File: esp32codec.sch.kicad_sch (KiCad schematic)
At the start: 8 parts, among them U13 TL072, U4 NAU88C22YG

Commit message: latest version
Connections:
- net Left IN: now reaches U4.3 (LLIN/GPIO2)
- net RIN: now reaches U4.6 (RLIN/GPIO3)
- net BCLK renamed i2sbclk
- net MLCK renamed i2s_lrck
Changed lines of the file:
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@@
+	(wire
+		(pts
+			(xy 85.09 95.25) (xy 93.98 95.25)
+		)
+		(stroke
+			(width 0)
+			(type default)
+		)
+	)
 	(wire
 		(pts
@@
 	(wire
 		(pts
+			(xy 80.01 97.79) (xy 93.98 97.79)
+		)
+		(stroke
+			(width 0)
+			(type default)
+		)
+	)
+	(wire
+		(pts
 			(xy 168.91 88.9) (xy 168.91 77.47)
 		)
@@
 		)
 	)
+	(hierarchical_label "RIN"
+		(shape input)
+		(at 80.01 97.79 180)
+		(effects
+			(font
+				(size 1.27 1.27)
+			)
+			(justify right)
+		)
+	)
 	(hierarchical_label "LRCK"
 		(shape input)
@@
 		)
 	)
-	(hierarchical_label "BCLK"
+	(hierarchical_label "i2sbclk"
 		(shape input)
 		(at 86.36 120.65 180)
+		(effects
+			(font
+				(size 1.27 1.27)
+			)
+			(justify right)
+		)
+	)
+	(hierarchical_label "Left IN"
+		(shape input)
+		(at 85.09 95.25 180)
 		(effects
 			(font
@@
 		)
 	)
-	(hierarchical_label "MLCK"
+	(hierarchical_label "i2s_lrck"
 		(shape input)
 		(at 83.82 132.08 180)

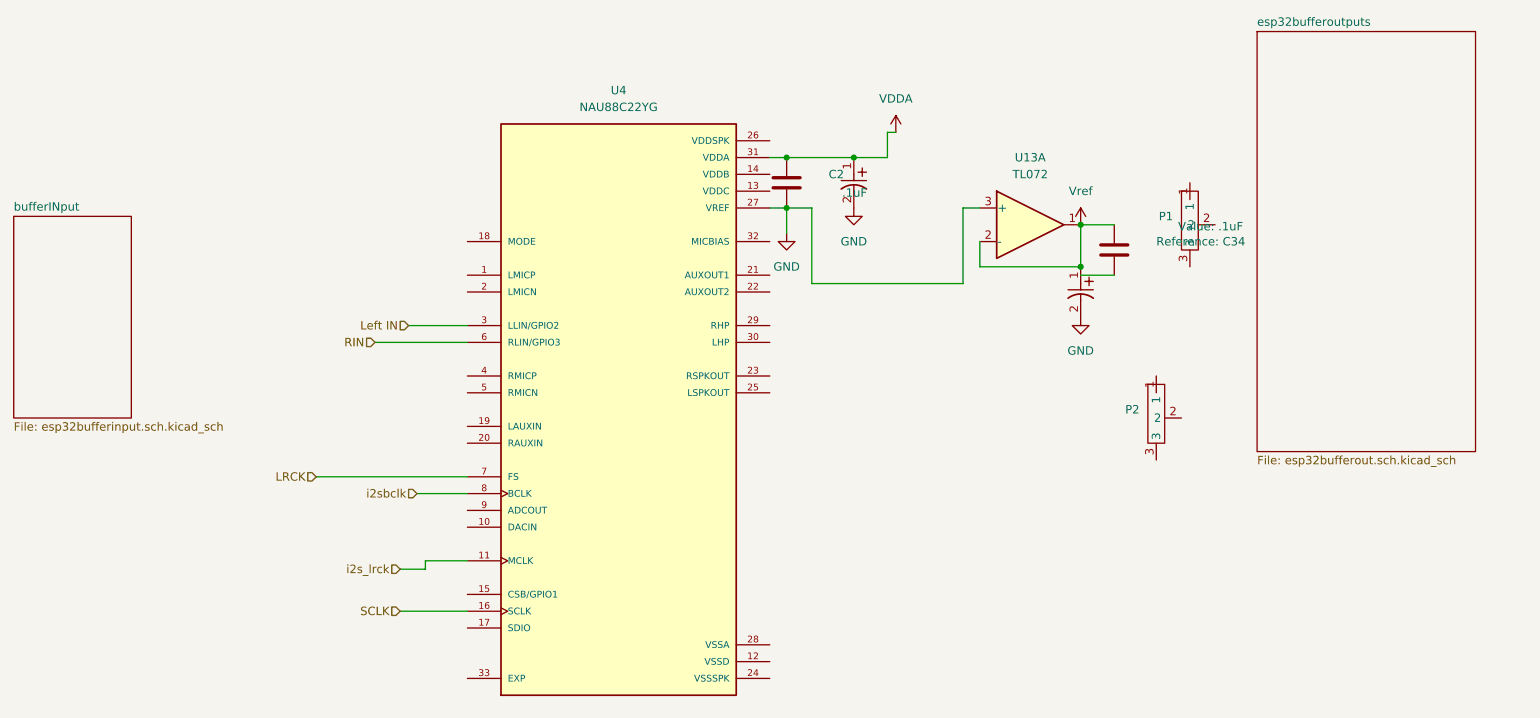
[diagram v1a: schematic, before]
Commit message: fixed up output buffers in codec schematic
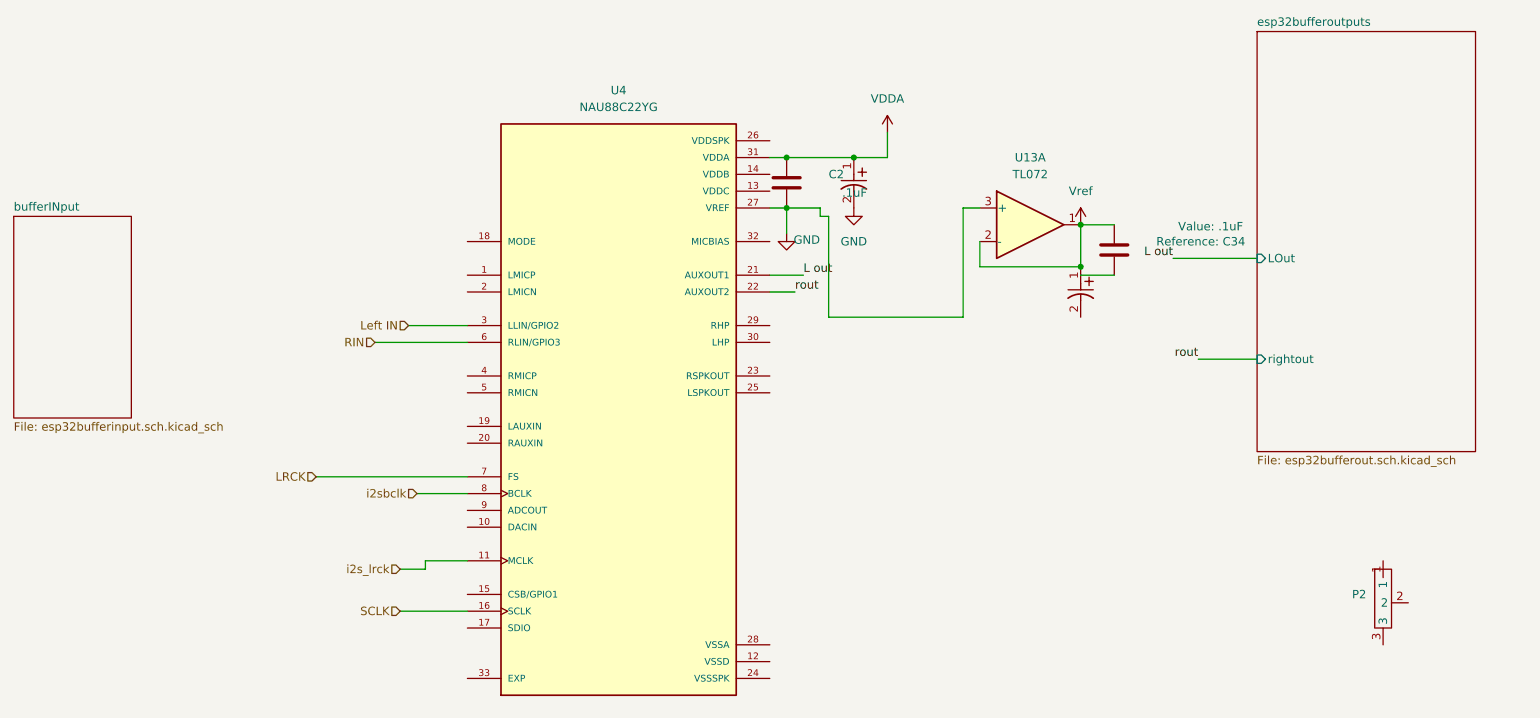
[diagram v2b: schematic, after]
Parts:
- removed P1: ~, 9mmsonghuie, symbol esp32lib:Pot
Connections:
- net GND: no longer C33.2
- net L out: now reaches U4.21 (AUXOUT1)
- net rout: now reaches U4.22 (AUXOUT2)
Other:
- sheet esp32bufferoutputs ports: added LOut, rightout; removed none
- moved on the sheet: P2
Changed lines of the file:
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@@
 	(wire
 		(pts
-			(xy 157.48 66.04) (xy 158.75 66.04)
-		)
-		(stroke
-			(width 0)
-			(type default)
-		)
-	)
-	(wire
-		(pts
-			(xy 142.24 77.47) (xy 146.05 77.47)
+			(xy 147.32 78.74) (xy 147.32 77.47)
+		)
+		(stroke
+			(width 0)
+			(type default)
+		)
+	)
+	(wire
+		(pts
+			(xy 143.51 90.17) (xy 139.7 90.17)
+		)
+		(stroke
+			(width 0)
+			(type default)
+		)
+	)
+	(wire
+		(pts
+			(xy 147.32 78.74) (xy 148.59 78.74)
 		)
 		(stroke
@@
 	(wire
 		(pts
+			(xy 147.32 77.47) (xy 142.24 77.47)
+		)
+		(stroke
+			(width 0)
+			(type default)
+		)
+	)
+	(wire
+		(pts
 			(xy 171.45 82.55) (xy 171.45 86.36)
 		)
@@
 	(wire
 		(pts
+			(xy 204.47 100.33) (xy 213.36 100.33)
+		)
+		(stroke
+			(width 0)
+			(type default)
+		)
+	)
+	(wire
+		(pts
 			(xy 139.7 77.47) (xy 142.24 77.47)
 		)
@@
 	(wire
 		(pts
-			(xy 146.05 88.9) (xy 168.91 88.9)
-		)
-		(stroke
-			(width 0)
-			(type default)
-		)
-	)
-	(wire
-		(pts
 			(xy 85.09 95.25) (xy 93.98 95.25)
 		)
@@
 	(wire
 		(pts
-			(xy 146.05 77.47) (xy 146.05 88.9)
+			(xy 213.36 85.09) (xy 200.66 85.09)
+		)
+		(stroke
+			(width 0)
+			(type default)
+		)
+	)
+	(wire
+		(pts
+			(xy 148.59 78.74) (xy 148.59 93.98)
 		)
 		(stroke
@@
 	(wire
 		(pts
-			(xy 168.91 88.9) (xy 168.91 77.47)
+			(xy 168.91 93.98) (xy 168.91 77.47)
+		)
+		(stroke
+			(width 0)
+			(type default)
+		)
+	)
+	(wire
+		(pts
+			(xy 148.59 93.98) (xy 168.91 93.98)
 		)
 		(stroke
@@
 			(width 0)
 			(type default)
+		)
+	)
+	(wire
+		(pts
+			(xy 144.78 87.63) (xy 139.7 87.63)
+		)
+		(stroke
+			(width 0)
+			(type default)
+		)
+	)
+	(label "L out"
+		(at 144.78 87.63 0)
+		(effects
+			(font
+				(size 1.27 1.27)
+			)
+			(justify left bottom)
+		)
+	)
+	(label "rout"
+		(at 143.51 90.17 0)
+		(effects
+			(font
+				(size 1.27 1.27)
+			)
+			(justify left bottom)
+		)
+	)
+	(label "rout"
+		(at 204.47 100.33 180)
+		(effects
+			(font
+				(size 1.27 1.27)
+			)
+			(justify right bottom)
+		)
+	)
+	(label "L out"
+		(at 200.66 85.09 180)
+		(effects
+			(font
+				(size 1.27 1.27)
+			)
+			(justify right bottom)
 		)
 	)
@@
 	(symbol
 		(lib_id "esp32lib:Pot")
-		(at 198.12 107.95 0)
+		(at 232.41 135.89 0)
 		(unit 1)
 		(exclude_from_sim no)
@@
 		(fields_autoplaced yes)
 		(property "Reference" "P2"
-			(at 195.58 107.9499 0)
+			(at 229.87 135.8899 0)
 			(effects
 				(font
@@
 		)
 		(property "Value" "~"
-			(at 195.58 109.855 0)
+			(at 229.87 137.795 0)
 			(effects
 				(font
@@
 		)
 		(property "Footprint" "9mmsonghuie"
-			(at 210.312 113.792 0)
+			(at 244.602 141.732 0)
 			(effects
 				(font
@@
 		)
 		(property "Datasheet" ""
-			(at 198.12 107.95 0)
+			(at 232.41 135.89 0)
 			(effects
 				(font
@@
 		)
 		(property "Description" ""
-			(at 198.12 107.95 0)
+			(at 232.41 135.89 0)
 			(effects
 				(font
@@
 	(symbol
 		(lib_id "power:VDDA")
-		(at 158.75 66.04 0)
+		(at 157.48 66.04 0)
 		(unit 1)
 		(exclude_from_sim no)
@@
 		(fields_autoplaced yes)
 		(property "Reference" "#PWR17"
-			(at 158.75 69.85 0)
+			(at 157.48 69.85 0)
 			(effects
 				(font
@@
 		)
 		(property "Value" "VDDA"
-			(at 158.75 60.96 0)
+			(at 157.48 60.96 0)
 			(effects
 				(font
@@
 		)
 		(property "Footprint" ""
-			(at 158.75 66.04 0)
+			(at 157.48 66.04 0)
 			(effects
 				(font
@@
 		)
 		(property "Datasheet" ""
-			(at 158.75 66.04 0)
+			(at 157.48 66.04 0)
 			(effects
 				(font
@@
 		)
 		(property "Description" "Power symbol creates a global label with name \"VDDA\""
-			(at 158.75 66.04 0)
+			(at 157.48 66.04 0)
 			(effects
 				(font
@@
 		(on_board yes)
 		(dnp no)
-		(fields_autoplaced yes)
 		(property "Reference" "#PWR19"
 			(at 142.24 87.63 0)
@@
 		)
 		(property "Value" "GND"
-			(at 142.24 86.36 0)
+			(at 145.288 82.296 0)
 			(effects
 				(font
@@
 		)
 	)
-	(symbol
-		(lib_id "power:GND")
-		(at 186.69 93.98 0)
-		(unit 1)
-		(exclude_from_sim no)
-		(in_bom yes)
-		(on_board yes)
-		(dnp no)
-		(fields_autoplaced yes)
-		(property "Reference" "#PWR71"
-			(at 186.69 100.33 0)
-			(effects
-				(font
-					(size 1.27 1.27)
-				)
-				(hide yes)
-			)
-		)
-		(property "Value" "GND"
-			(at 186.69 99.06 0)
-			(effects
-				(font
-					(size 1.27 1.27)
-				)
-			)
-		)
-		(property "Footprint" ""
-			(at 186.69 93.98 0)
-			(effects
-				(font
-					(size 1.27 1.27)
-				)
-				(hide yes)
-			)
-		)
-		(property "Datasheet" ""
-			(at 186.69 93.98 0)
-			(effects
-				(font
-					(size 1.27 1.27)
-				)
-				(hide yes)
-			)
-		)
-		(property "Description" "Power symbol creates a global label with name \"GND\" , ground"
-			(at 186.69 93.98 0)
-			(effects
-				(font
-					(size 1.27 1.27)
-				)
-				(hide yes)
-			)
-		)
-		(pin "1"
-		)
-		(instances
-			(project ""
-				(path "/c4754426-a41b-4341-9d09-2e389619f3d6/32d637b3-b81c-4082-b7fa-739e0cc157fd"
-					(reference "#PWR71")
-					(unit 1)
-				)
-			)
-		)
-	)
-	(symbol
-		(lib_id "esp32lib:Pot")
-		(at 203.2 78.74 0)
-		(unit 1)
-		(exclude_from_sim no)
-		(in_bom yes)
-		(on_board yes)
-		(dnp no)
-		(fields_autoplaced yes)
-		(property "Reference" "P1"
-			(at 200.66 78.7399 0)
-			(effects
-				(font
-					(size 1.27 1.27)
-				)
-				(justify right)
-			)
-		)
-		(property "Value" "~"
-			(at 200.66 80.645 0)
-			(effects
-				(font
-					(size 1.27 1.27)
-				)
-				(justify right)
-			)
-		)
-		(property "Footprint" "9mmsonghuie"
-			(at 215.392 84.582 0)
-			(effects
-				(font
-					(size 1.27 1.27)
-				)
-				(hide yes)
-			)
-		)
-		(property "Datasheet" ""
-			(at 203.2 78.74 0)
-			(effects
-				(font
-					(size 1.27 1.27)
-				)
-				(hide yes)
-			)
-		)
-		(property "Description" ""
-			(at 203.2 78.74 0)
-			(effects
-				(font
-					(size 1.27 1.27)
-				)
-				(hide yes)
-			)
-		)
-		(pin "3"
-		)
-		(pin "2"
-		)
-		(pin "1"
-		)
-		(instances
-			(project ""
-				(path "/c4754426-a41b-4341-9d09-2e389619f3d6/32d637b3-b81c-4082-b7fa-739e0cc157fd"
-					(reference "P1")
-					(unit 1)
-				)
-			)
-		)
-	)
 	(sheet
 		(at 213.36 50.8)
@@
 			)
 		)
+		(pin "LOut" input
+			(at 213.36 85.09 180)
+			(effects
+				(font
+					(size 1.27 1.27)
+				)
+				(justify left)
+			)
+		)
+		(pin "rightout" input
+			(at 213.36 100.33 180)
+			(effects
+				(font
+					(size 1.27 1.27)
+				)
+				(justify left)
+			)
+		)

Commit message: aded an stmsheet to see the symbol
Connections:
- net GND: now also C33.2; no longer U13.3 (+), U4.27 (VREF)
- new net vref: U13.3 (+), U4.27 (VREF)
- no-connect marks 0 -> 11
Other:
- moved on the sheet: C2, U13A

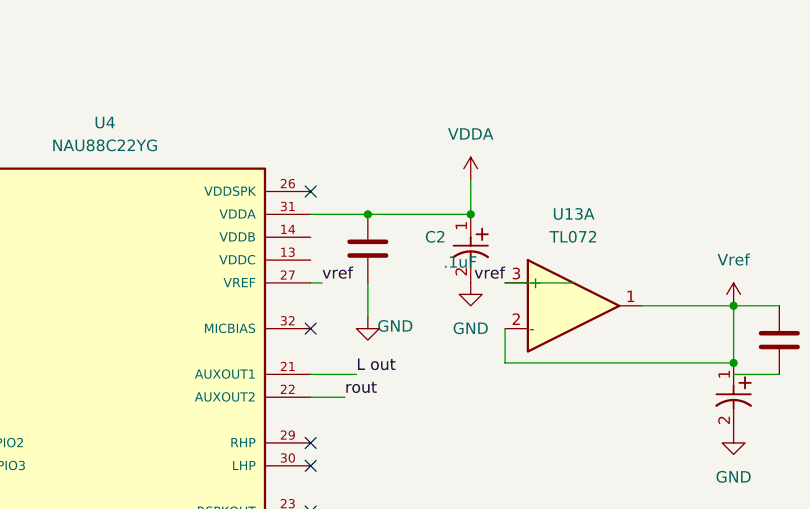
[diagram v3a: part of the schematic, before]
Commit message: more codec wiring
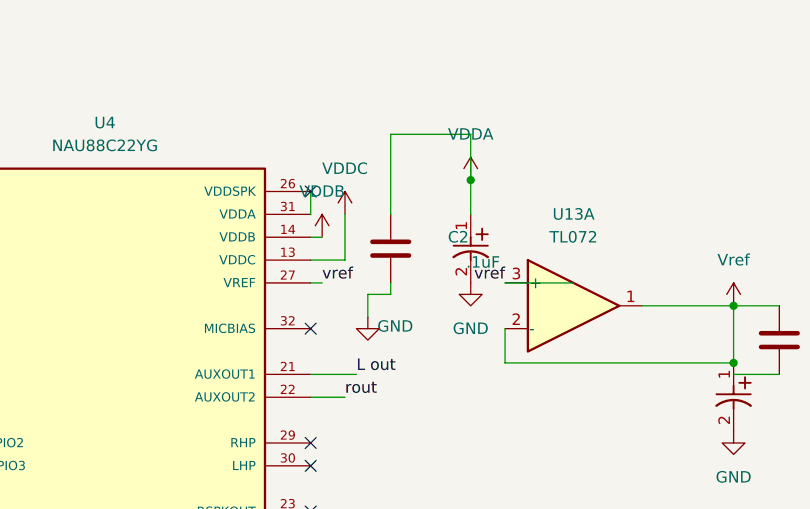
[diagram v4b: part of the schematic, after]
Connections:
- net VDDA: no longer U4.31 (VDDA)
- net VDDC: now reaches U4.13 (VDDC)
- net VDDB: now reaches U4.14 (VDDB)
- net at U4.26 (VDDSPK): now also U4.31 (VDDA)
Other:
- moved on the sheet: C2
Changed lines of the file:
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@@
+	)
+	(junction
+		(at 157.48 66.04)
+		(diameter 0)
+		(color 0 0 0 0)
 	)
 	(junction
@@
 		(color 0 0 0 0)
 	)
-	(junction
-		(at 146.05 69.85)
-		(diameter 0)
-		(color 0 0 0 0)
-	)
-	(junction
-		(at 157.48 69.85)
-		(diameter 0)
-		(color 0 0 0 0)
-	)
 	(no_connect
 		(at 93.98 113.03)
@@
 	(wire
 		(pts
-			(xy 146.05 69.85) (xy 157.48 69.85)
+			(xy 148.59 60.96) (xy 157.48 60.96)
 		)
 		(stroke
@@
 	(wire
 		(pts
+			(xy 148.59 60.96) (xy 148.59 69.85)
+		)
+		(stroke
+			(width 0)
+			(type default)
+		)
+	)
+	(wire
+		(pts
 			(xy 186.69 80.01) (xy 191.77 80.01)
 		)
@@
 	(wire
 		(pts
-			(xy 139.7 69.85) (xy 146.05 69.85)
-		)
-		(stroke
-			(width 0)
-			(type default)
-		)
-	)
-	(wire
-		(pts
 			(xy 71.12 118.11) (xy 93.98 118.11)
 		)
@@
 	(wire
 		(pts
+			(xy 146.05 78.74) (xy 146.05 81.28)
+		)
+		(stroke
+			(width 0)
+			(type default)
+		)
+	)
+	(wire
+		(pts
 			(xy 204.47 100.33) (xy 213.36 100.33)
 		)
@@
 	(wire
 		(pts
+			(xy 157.48 60.96) (xy 157.48 66.04)
+		)
+		(stroke
+			(width 0)
+			(type default)
+		)
+	)
+	(wire
+		(pts
 			(xy 86.36 120.65) (xy 93.98 120.65)
 		)
@@
 	(wire
 		(pts
+			(xy 139.7 67.31) (xy 139.7 69.85)
+		)
+		(stroke
+			(width 0)
+			(type default)
+		)
+	)
+	(wire
+		(pts
 			(xy 186.69 86.36) (xy 186.69 80.01)
 		)
@@
 	(wire
 		(pts
+			(xy 139.7 72.39) (xy 140.97 72.39)
+		)
+		(stroke
+			(width 0)
+			(type default)
+		)
+	)
+	(wire
+		(pts
 			(xy 213.36 85.09) (xy 200.66 85.09)
 		)
@@
 	(wire
 		(pts
-			(xy 146.05 81.28) (xy 146.05 77.47)
+			(xy 148.59 78.74) (xy 146.05 78.74)
+		)
+		(stroke
+			(width 0)
+			(type default)
+		)
+	)
+	(wire
+		(pts
+			(xy 143.51 74.93) (xy 143.51 69.85)
+		)
+		(stroke
+			(width 0)
+			(type default)
+		)
+	)
+	(wire
+		(pts
+			(xy 148.59 78.74) (xy 148.59 77.47)
 		)
 		(stroke
@@
 		(pts
 			(xy 80.01 97.79) (xy 93.98 97.79)
+		)
+		(stroke
+			(width 0)
+			(type default)
+		)
+	)
+	(wire
+		(pts
+			(xy 139.7 74.93) (xy 143.51 74.93)
 		)
 		(stroke
@@
 	)
 	(symbol
+		(lib_id "power:VDDA")
+		(at 143.51 69.85 0)
+		(unit 1)
+		(exclude_from_sim no)
+		(in_bom yes)
+		(on_board yes)
+		(dnp no)
+		(fields_autoplaced yes)
+		(property "Reference" "#PWR82"
+			(at 143.51 73.66 0)
+			(effects
+				(font
+					(size 1.27 1.27)
+				)
+				(hide yes)
+			)
+		)
+		(property "Value" "VDDC"
+			(at 143.51 64.77 0)
+			(effects
+				(font
+					(size 1.27 1.27)
+				)
+			)
+		)
+		(property "Footprint" ""
+			(at 143.51 69.85 0)
+			(effects
+				(font
+					(size 1.27 1.27)
+				)
+				(hide yes)
+			)
+		)
+		(property "Datasheet" ""
+			(at 143.51 69.85 0)
+			(effects
+				(font
+					(size 1.27 1.27)
+				)
+				(hide yes)
+			)
+		)
+		(property "Description" "Power symbol creates a global label with name \"VDDA\""
+			(at 143.51 69.85 0)
+			(effects
+				(font
+					(size 1.27 1.27)
+				)
+				(hide yes)
+			)
+		)
+		(pin "1"
+		)
+		(instances
+			(project "esp32"
+				(path "/c4754426-a41b-4341-9d09-2e389619f3d6/32d637b3-b81c-4082-b7fa-739e0cc157fd"
+					(reference "#PWR82")
+					(unit 1)
+				)
+			)
+		)
+	)
+	(symbol
 		(lib_id "esp32lib:T491C106M025AT7280")
 		(at 186.69 86.36 270)
@@
 	)
 	(symbol
-		(lib_id "power:VDDA")
-		(at 157.48 66.04 0)
-		(unit 1)
-		(exclude_from_sim no)
-		(in_bom yes)
-		(on_board yes)
-		(dnp no)
-		(fields_autoplaced yes)
-		(property "Reference" "#PWR17"
-			(at 157.48 69.85 0)
-			(effects
-				(font
-					(size 1.27 1.27)
-				)
-				(hide yes)
-			)
-		)
-		(property "Value" "VDDA"
-			(at 157.48 60.96 0)
-			(effects
-				(font
-					(size 1.27 1.27)
-				)
-			)
-		)
-		(property "Footprint" ""
-			(at 157.48 66.04 0)
-			(effects
-				(font
-					(size 1.27 1.27)
-				)
-				(hide yes)
-			)
-		)
-		(property "Datasheet" ""
-			(at 157.48 66.04 0)
-			(effects
-				(font
-					(size 1.27 1.27)
-				)
-				(hide yes)
-			)
-		)
-		(property "Description" "Power symbol creates a global label with name \"VDDA\""
-			(at 157.48 66.04 0)
-			(effects
-				(font
-					(size 1.27 1.27)
-				)
-				(hide yes)
-			)
-		)
-		(pin "1"
-		)
-		(instances
-			(project ""
-				(path "/c4754426-a41b-4341-9d09-2e389619f3d6/32d637b3-b81c-4082-b7fa-739e0cc157fd"
-					(reference "#PWR17")
-					(unit 1)
-				)
-			)
-		)
-	)
-	(symbol
 		(lib_id "power:GND")
 		(at 146.05 81.28 0)
@@
 	)
 	(symbol
+		(lib_id "power:VDDA")
+		(at 157.48 66.04 0)
+		(unit 1)
+		(exclude_from_sim no)
+		(in_bom yes)
+		(on_board yes)
+		(dnp no)
+		(fields_autoplaced yes)
+		(property "Reference" "#PWR17"
+			(at 157.48 69.85 0)
+			(effects
+				(font
+					(size 1.27 1.27)
+				)
+				(hide yes)
+			)
+		)
+		(property "Value" "VDDA"
+			(at 157.48 60.96 0)
+			(effects
+				(font
+					(size 1.27 1.27)
+				)
+			)
+		)
+		(property "Footprint" ""
+			(at 157.48 66.04 0)
+			(effects
+				(font
+					(size 1.27 1.27)
+				)
+				(hide yes)
+			)
+		)
+		(property "Datasheet" ""
+			(at 157.48 66.04 0)
+			(effects
+				(font
+					(size 1.27 1.27)
+				)
+				(hide yes)
+			)
+		)
+		(property "Description" "Power symbol creates a global label with name \"VDDA\""
+			(at 157.48 66.04 0)
+			(effects
+				(font
+					(size 1.27 1.27)
+				)
+				(hide yes)
+			)
+		)
+		(pin "1"
+		)
+		(instances
+			(project ""
+				(path "/c4754426-a41b-4341-9d09-2e389619f3d6/32d637b3-b81c-4082-b7fa-739e0cc157fd"
+					(reference "#PWR17")
+					(unit 1)
+				)
+			)
+		)
+	)
+	(symbol
 		(lib_id "modcaneuro:NAU88C22YG")
 		(at 116.84 107.95 0)
@@
 	(symbol
 		(lib_id "Device:C")
-		(at 146.05 73.66 0)
+		(at 148.59 73.66 0)
 		(unit 1)
 		(exclude_from_sim no)
@@
 		(dnp no)
 		(property "Reference" "C2"
-			(at 152.4 72.3899 0)
+			(at 154.94 72.3899 0)
 			(effects
 				(font
@@
 		)
 		(property "Value" ".1uF"
-			(at 154.432 75.184 0)
+			(at 156.972 75.184 0)
 			(effects
 				(font
@@
 		)
 		(property "Footprint" "Capacitor_SMD:C_0201_0603Metric"
-			(at 147.0152 77.47 0)
+			(at 149.5552 77.47 0)
 			(effects
 				(font
@@
 		)
 		(property "Datasheet" "~"
-			(at 146.05 73.66 0)
+			(at 148.59 73.66 0)
 			(effects
 				(font
@@
 		)
 		(property "Description" "Unpolarized capacitor"
-			(at 146.05 73.66 0)
+			(at 148.59 73.66 0)
 			(effects
 				(font
@@
 					(unit 1)
 				)
+			)
+		)
+	)
+	(symbol
+		(lib_id "power:VDDA")
+		(at 140.97 72.39 0)
+		(unit 1)
+		(exclude_from_sim no)
+		(in_bom yes)
+		(on_board yes)
+		(dnp no)
+		(fields_autoplaced yes)
+		(property "Reference" "#PWR81"
+			(at 140.97 76.2 0)
+			(effects
+				(font
+					(size 1.27 1.27)
+				)
+				(hide yes)
+			)
+		)
+		(property "Value" "VDDB"
+			(at 140.97 67.31 0)
+			(effects
+				(font
+					(size 1.27 1.27)
+				)
+			)
+		)
+		(property "Footprint" ""
+			(at 140.97 72.39 0)
+			(effects
+				(font
+					(size 1.27 1.27)
+				)
+				(hide yes)
+			)
+		)
+		(property "Datasheet" ""
+			(at 140.97 72.39 0)
+			(effects
+				(font
+					(size 1.27 1.27)
+				)
+				(hide yes)
+			)
+		)
+		(property "Description" "Power symbol creates a global label with name \"VDDA\""
+			(at 140.97 72.39 0)
+			(effects
+				(font
+					(size 1.27 1.27)
+				)
+				(hide yes)
+			)
+		)
+		(pin "1"
+		)
+		(instances
+			(project "esp32"
+				(path "/c4754426-a41b-4341-9d09-2e389619f3d6/32d637b3-b81c-4082-b7fa-739e0cc157fd"
+					(reference "#PWR81")
+					(unit 1)
+				)
